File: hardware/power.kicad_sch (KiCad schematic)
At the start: 100 parts, among them J3 Vcore_sel, U1 TLV62569DBV, U2 TLV62569DBV, U3 MPM3833CGRH-Z, U4 CCGM1A1, U5 TLV62569DBV, U6 TLV62569DBV

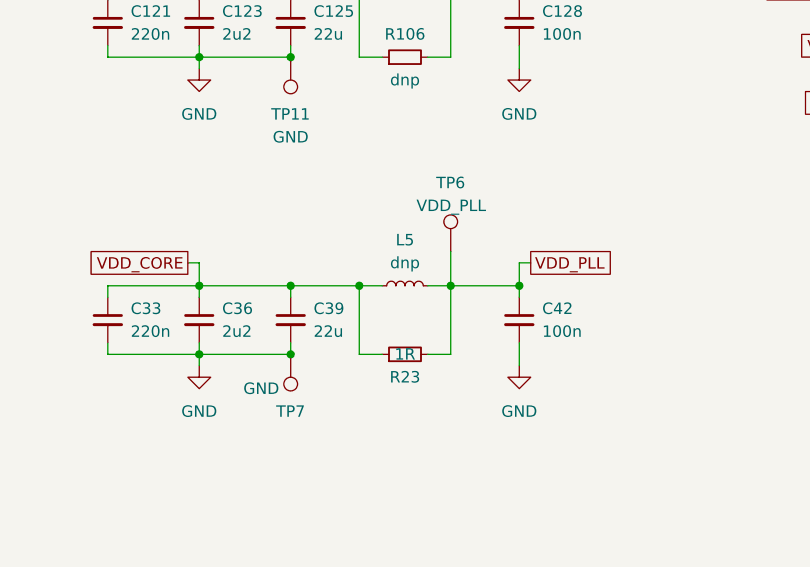
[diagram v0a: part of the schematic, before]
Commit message: Routing BTNs, LEDs, CLK
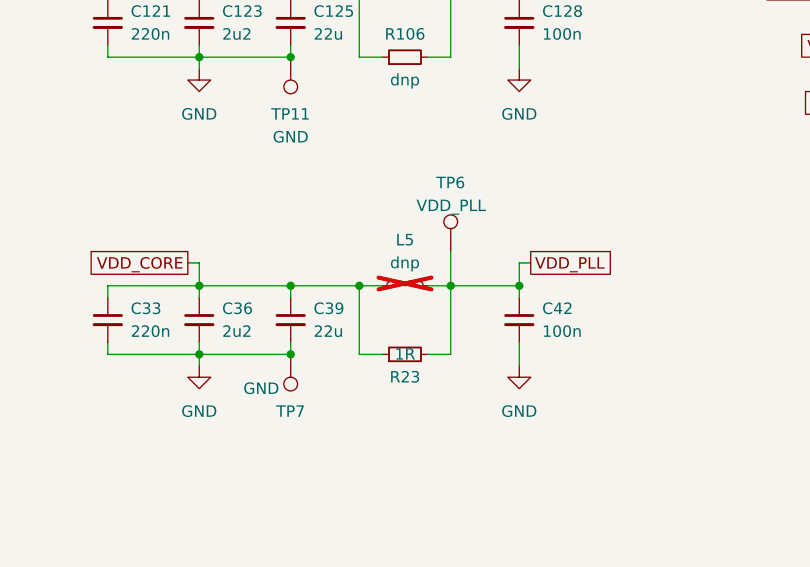
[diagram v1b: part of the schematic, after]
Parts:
- L5: now not fitted; now left out of the parts list
- L6, L7: footprint (none) -> Inductor_SMD:L_0603_1608Metric
- U3: footprint (none) -> ulx5m-gs:MPM3833CGRH-Z
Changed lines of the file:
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@@
 			)
 		)
-		(property "Footprint" ""
+		(property "Footprint" "Inductor_SMD:L_0603_1608Metric"
 			(at 161.29 76.2 0)
 			(effects
@@
 		(at 161.29 142.24 90)
 		(unit 1)
-		(exclude_from_sim no)
-		(in_bom yes)
-		(on_board yes)
-		(dnp no)
+		(exclude_from_sim yes)
+		(in_bom no)
+		(on_board no)
+		(dnp yes)
 		(fields_autoplaced yes)
 		(property "Reference" "L5"
@@
 			)
 		)
-		(property "Footprint" ""
+		(property "Footprint" "Inductor_SMD:L_0603_1608Metric"
 			(at 161.29 109.22 0)
 			(effects
@@
 			)
 		)
-		(property "Footprint" ""
+		(property "Footprint" "ulx5m-gs:MPM3833CGRH-Z"
 			(at 63.5 24.384 0)
 			(effects

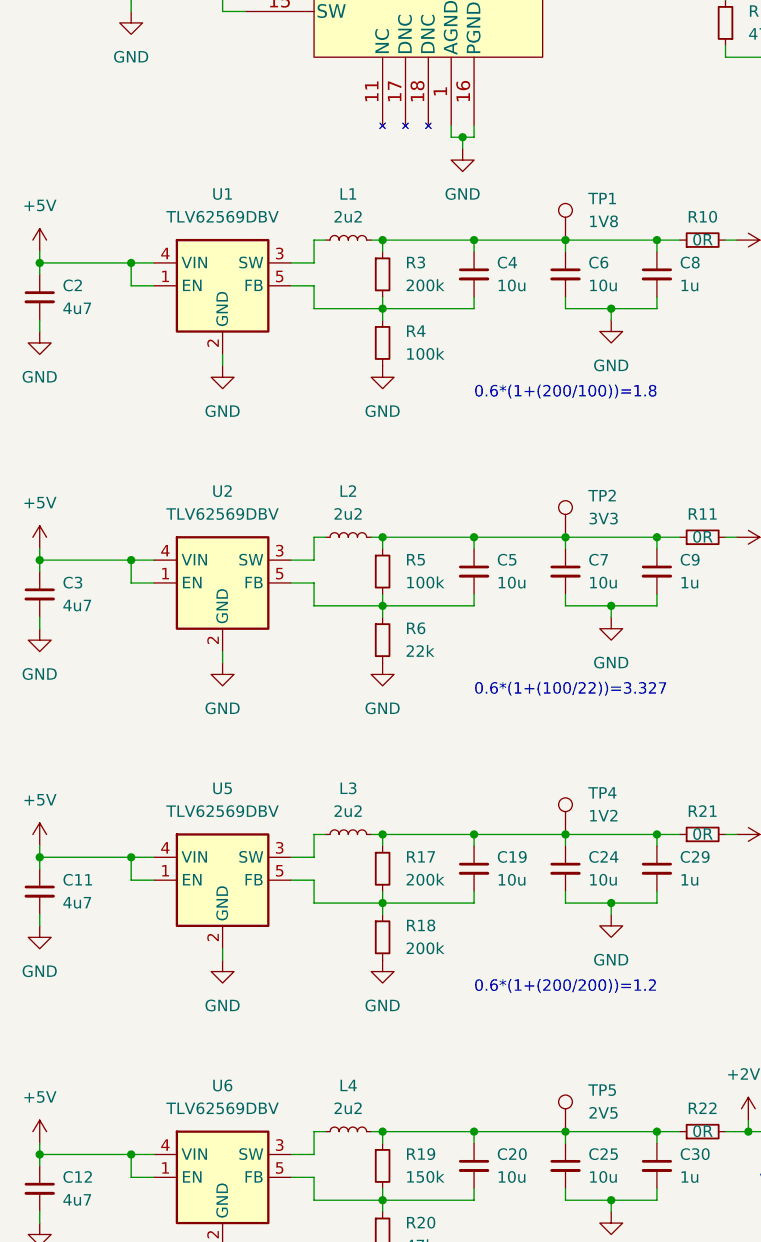
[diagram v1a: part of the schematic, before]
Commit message: Adding L1, L2, L3, L4 FB1,FB2, FB3 parts, changing name under FPGA
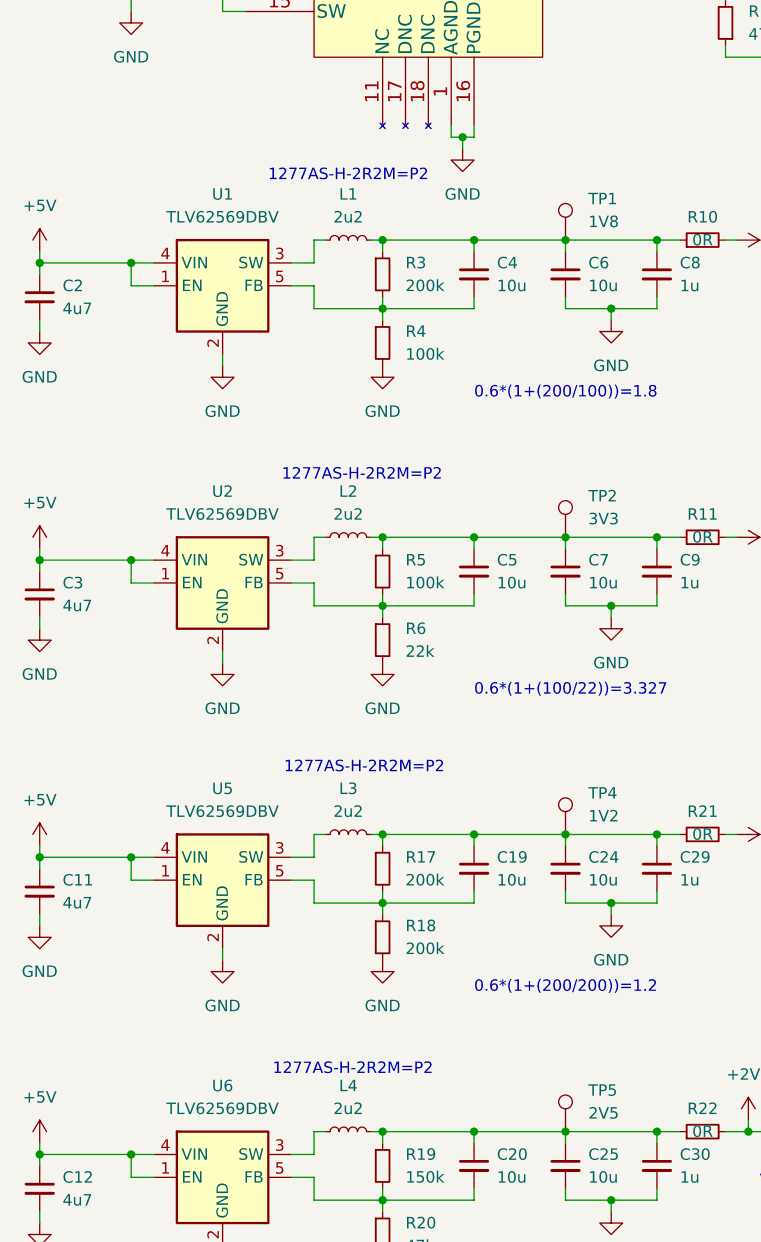
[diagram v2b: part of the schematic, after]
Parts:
- L1, L2, L3, L4: Mouser (none) -> https://hr.mouser.com/ProductDetail/Murata-Electronics/1277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
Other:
- note added: "1277AS-H-2R2M=P2"
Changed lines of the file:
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@@
 		)
 	)
+	(text "1277AS-H-2R2M=P2"
+		(exclude_from_sim no)
+		(at 54.61 69.088 0)
+		(effects
+			(font
+				(size 1.27 1.27)
+			)
+		)
+	)
+	(text "1277AS-H-2R2M=P2"
+		(exclude_from_sim no)
+		(at 56.388 134.874 0)
+		(effects
+			(font
+				(size 1.27 1.27)
+			)
+		)
+	)
 	(text "0.6*(1+(150/47))=2.515"
 		(exclude_from_sim no)
@@
 		)
 	)
+	(text "1277AS-H-2R2M=P2"
+		(exclude_from_sim no)
+		(at 55.118 168.402 0)
+		(effects
+			(font
+				(size 1.27 1.27)
+			)
+		)
+	)
+	(text "1277AS-H-2R2M=P2"
+		(exclude_from_sim no)
+		(at 56.134 102.362 0)
+		(effects
+			(font
+				(size 1.27 1.27)
+			)
+		)
+	)
 	(junction
 		(at 68.58 109.22)
@@
 			)
 		)
+		(property "Mouser" "https://hr.mouser.com/ProductDetail/Murata-Electronics/1277AS-H-2R2M%3dP2?qs=4tuKoHGzn104DGWhEjLPYA%3D%3D"
+			(at 54.61 175.26 0)
+			(effects
+				(font
+					(size 1.27 1.27)
+				)
+				(hide yes)
+			)
+		)
 		(pin "1"
 		)
@@
 			)
 		)
+		(property "Mouser" "https://hr.mouser.com/ProductDetail/Murata-Electronics/1277AS-H-2R2M%3dP2?qs=4tuKoHGzn104DGWhEjLPYA%3D%3D"
+			(at 54.61 109.22 0)
+			(effects
+				(font
+					(size 1.27 1.27)
+				)
+				(hide yes)
+			)
+		)
 		(pin "1"
 		)
@@
 			)
 		)
+		(property "Mouser" "https://hr.mouser.com/ProductDetail/Murata-Electronics/1277AS-H-2R2M%3dP2?qs=4tuKoHGzn104DGWhEjLPYA%3D%3D"
+			(at 54.61 76.2 0)
+			(effects
+				(font
+					(size 1.27 1.27)
+				)
+				(hide yes)
+			)
+		)
 		(pin "1"
 		)
@@
 			)
 		)
+		(property "Mouser" "https://hr.mouser.com/ProductDetail/Murata-Electronics/1277AS-H-2R2M%3dP2?qs=4tuKoHGzn104DGWhEjLPYA%3D%3D"
+			(at 54.61 142.24 0)
+			(effects
+				(font
+					(size 1.27 1.27)
+				)
+				(hide yes)
+			)
+		)

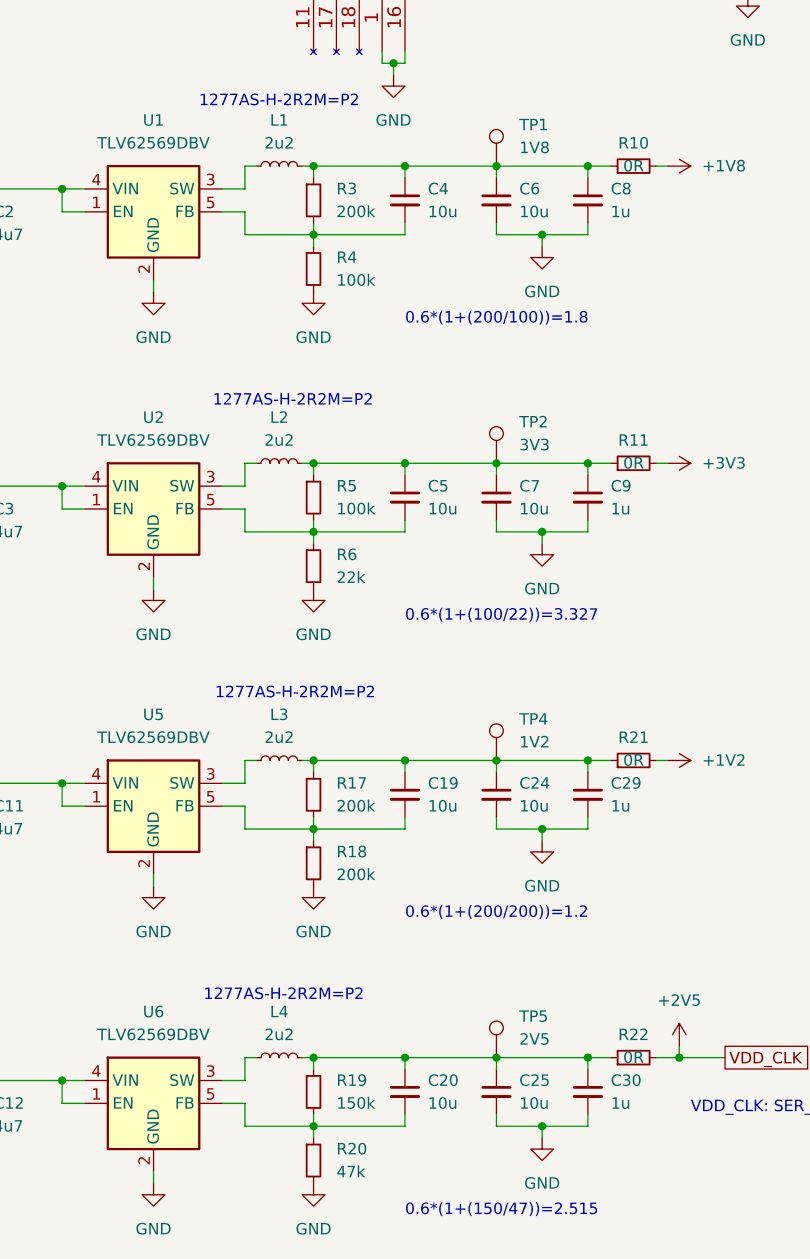
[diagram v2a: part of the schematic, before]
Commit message: Switching A and B on TXS0202YZPR adding pass resistors
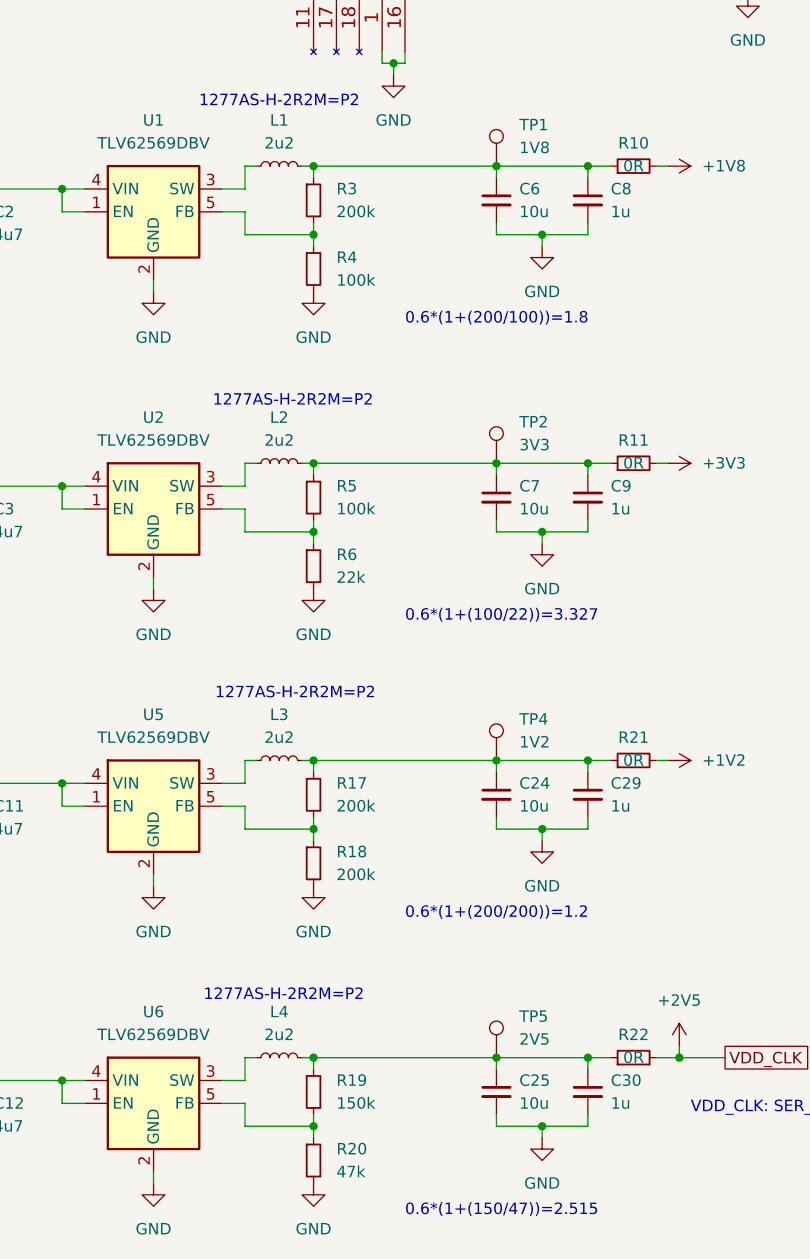
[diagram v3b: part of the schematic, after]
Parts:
- removed C19, C20, C4, C5: 10u, Capacitor_SMD:C_0402_1005Metric, symbol Device:C_Small

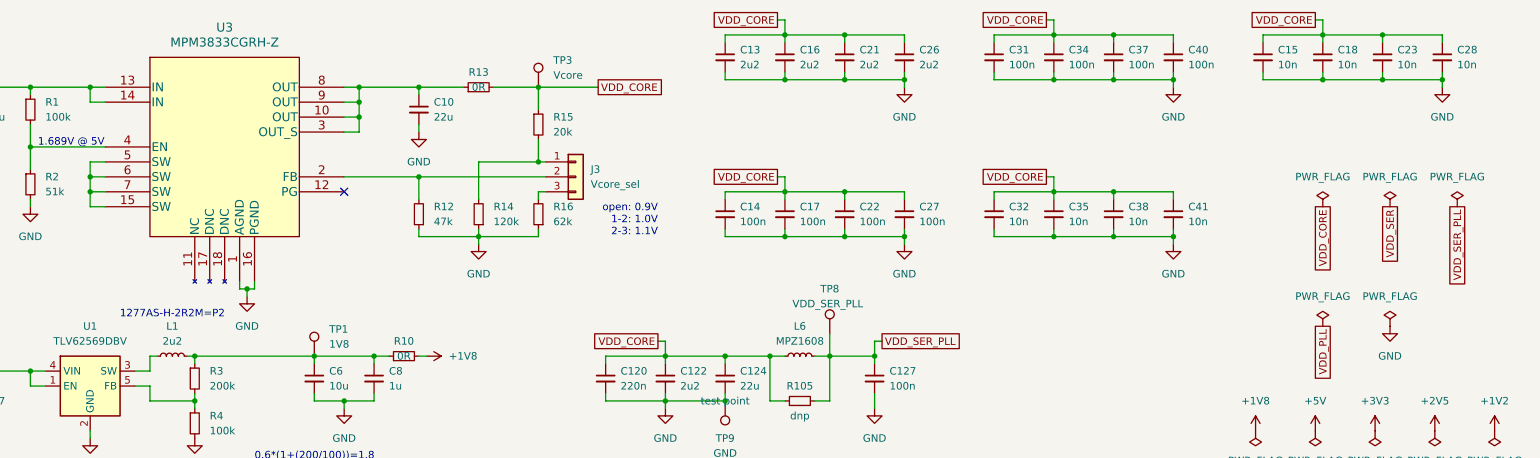
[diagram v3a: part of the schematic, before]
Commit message: #2 should be cleared now
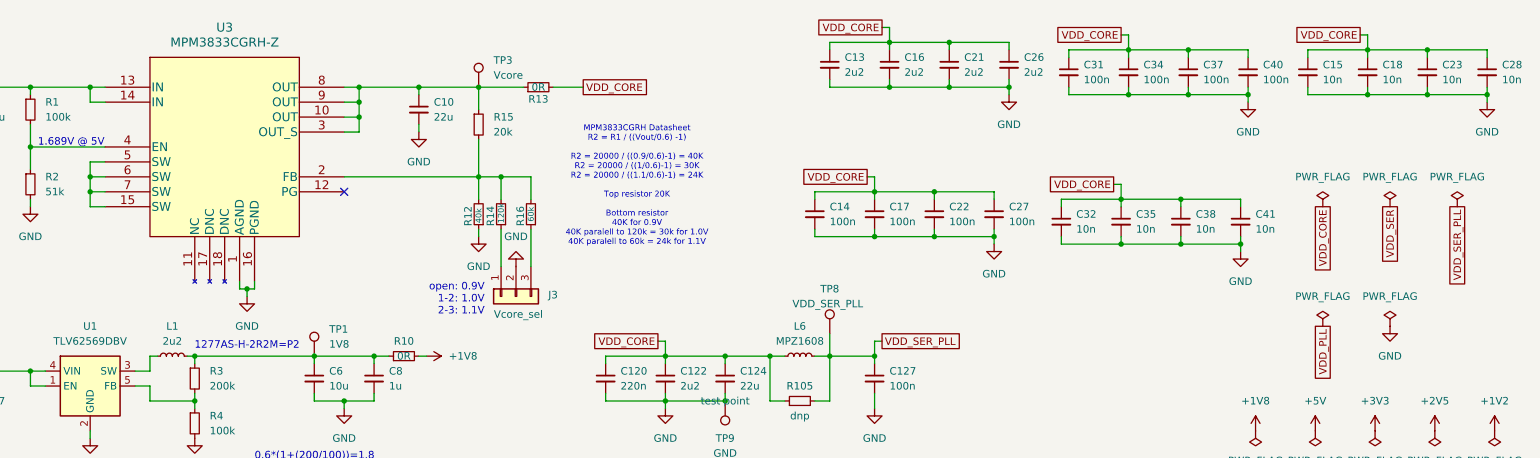
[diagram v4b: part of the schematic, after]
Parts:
- C1, C10: footprint Capacitor_SMD:C_0402_1005Metric -> Capacitor_SMD:C_0805_2012Metric
- R12: value 47k -> 40k
- R16: value 62k -> 60k
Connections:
- net GND: now also J3.2 (Pin_2); no longer R14.1, R16.1
- net VDD_CORE: no longer R15.1, TP3.1
- net at C10.1, R13.1, U3.10 (OUT)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: now also R15.1, TP3.1
- net at J3.3 (Pin_3): now also R16.1; no longer R16.2
- net at R14.2, R15.2: now also R12.2, R16.2, U3.2 (FB); no longer J3.1 (Pin_1)
- new net: J3.1 (Pin_1), R14.1
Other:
- note added: "MPM3833CGRH Datasheet R2 = R1 / ((Vout/0.6) -1) R2 = 20000 / ((0.9/0.6)-1) = 40K R2 = 20000 / ((1/0.6)-1) = 30K R2 = 20000 / ((1.1/0.6)-1) = 24K Top resistor 20K Bottom resistor 40K for 0.9V 40K paralell to 120k = 30k for 1.0V 40K paralell to 60k = 24k for 1.1V"
- moved on the sheet: C13, C14, C15, C16, C17, C18, C21, C22, C23, C26, C27, C28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
